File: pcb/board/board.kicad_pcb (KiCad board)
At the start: 2 copper layers, 6 parts, among them J1 Screw_Terminal_01x03, J2 Screw_Terminal_01x03, J3 Screw_Terminal_01x03, J5 Screw_Terminal_01x03

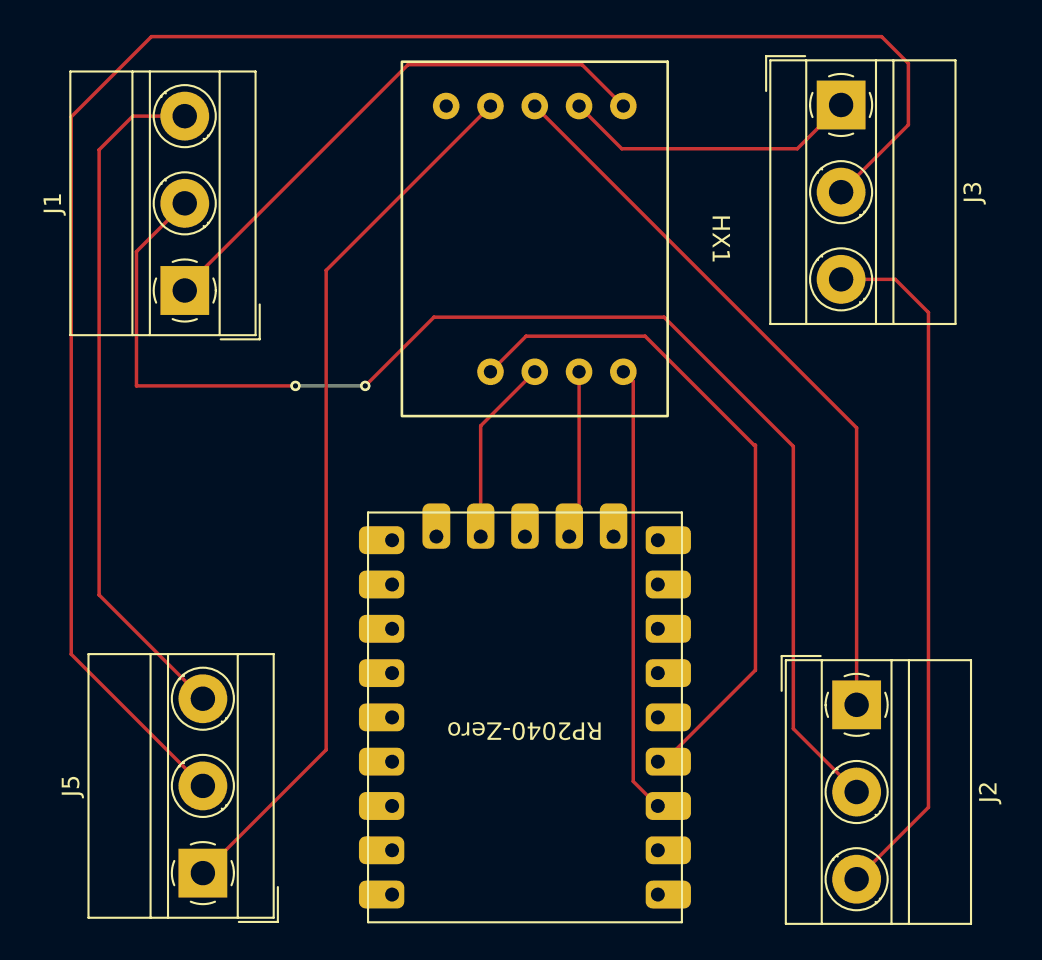
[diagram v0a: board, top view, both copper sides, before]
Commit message: wip work on the load cell part
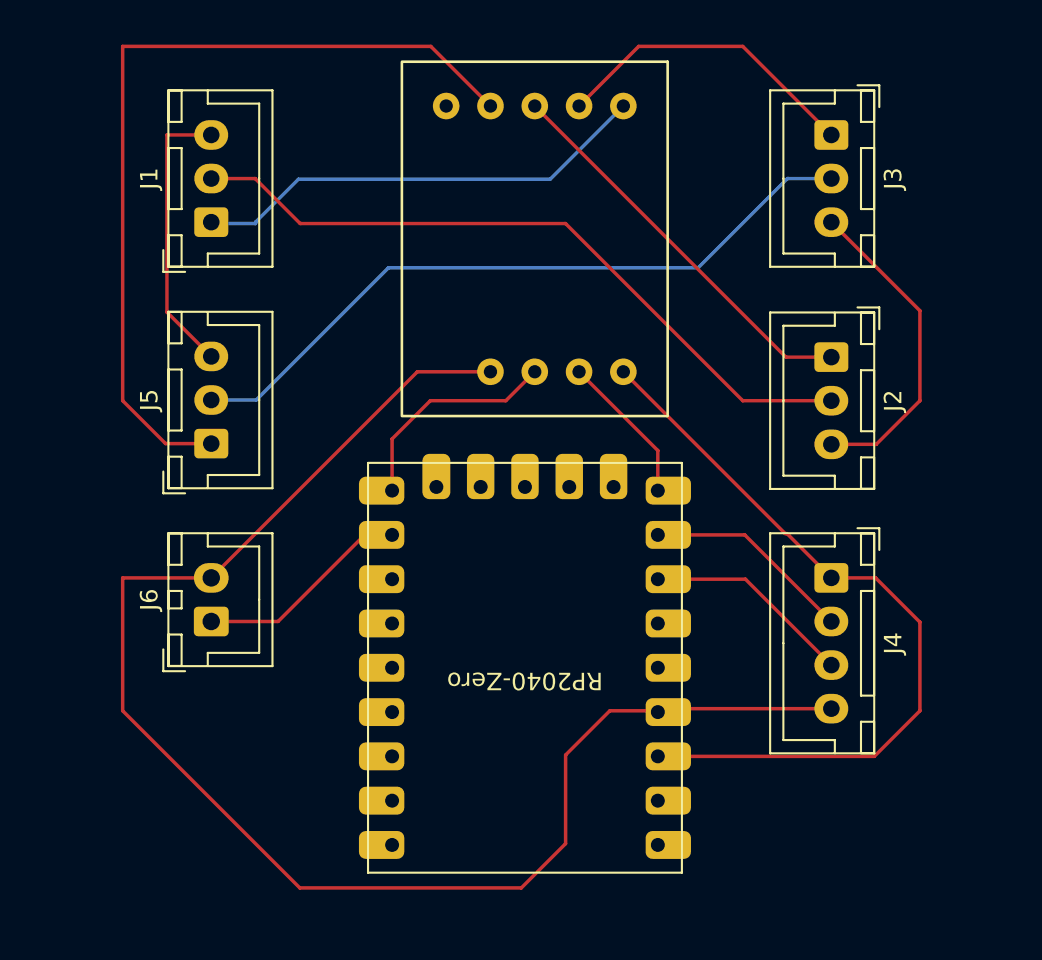
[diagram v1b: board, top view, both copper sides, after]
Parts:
- added J4: Screw_Terminal_01x04, Connector_JST:JST_XH_B4B-XH-A_1x04_P2.50mm_Vertical, F.Cu at (167.6, 66.0)
- added J6: Screw_Terminal_01x02, Connector_JST:JST_XH_B2B-XH-A_1x02_P2.50mm_Vertical, F.Cu at (132.1, 68.5)
- J1, J2, J3, J5: footprint TerminalBlock_MetzConnect:TerminalBlock_MetzConnect_Type011_RT05503HBWC_1x03_P5.00mm_Horizontal -> Connector_JST:JST_XH_B3B-XH-A_1x03_P2.50mm_Vertical
- moved J5 24.6 mm to (132.1, 58.3)
- moved J2 20.0 mm to (167.6, 53.4)
- moved J1 4.20 mm to (132.1, 45.6)
- moved RZ1 2.85 mm to (160.2, 58.5)
- moved J3 1.81 mm to (167.6, 40.6)
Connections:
- net Net-(HX1-2.7-5v) renamed 3V3
- net Net-(HX1-GND) renamed GND
- RZ1 pad 11: Net-(HX1-CLK) -> unconnected-(RZ1-GP10-Pad11)
- RZ1 pad 13: Net-(HX1-DAT) -> unconnected-(RZ1-GP12-Pad13)
- RZ1 pad 15: unconnected-(RZ1-GP14-Pad15) -> Net-(HX1-DAT)
- RZ1 pad 16: unconnected-(RZ1-GP15-Pad16) -> Net-(J4-Pin_2)
- RZ1 pad 17: unconnected-(RZ1-GP26-Pad17) -> Net-(J4-Pin_3)
- RZ1 pad 8: unconnected-(RZ1-GP7-Pad8) -> Net-(J6-Pin_1)
- RZ1 pad 9: unconnected-(RZ1-GP8-Pad9) -> Net-(HX1-CLK)
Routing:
- net Net-(J3-Pin_2): track 101.0 -> 40.8 mm
- net GND: track 39.3 -> 85.8 mm
- net Net-(J1-Pin_2): track 75.4 -> 40.8 mm, vias 2 -> 0
- net Net-(J1-Pin_3): track 39.7 -> 16.3 mm
- net Net-(J2-Pin_3): track 40.0 -> 18.5 mm
- net Net-(HX1-WHT/A-): track 42.0 -> 23.0 mm
- net 3V3: track 25.7 -> 44.1 mm
- net Net-(J6-Pin_1): track 0.00 -> 12.4 mm
- net Net-(J4-Pin_2): track 0.00 -> 12.0 mm
- net Net-(J4-Pin_3): track 0.00 -> 12.0 mm
- net Net-(HX1-RED/E+): track 31.4 -> 26.5 mm
- net Net-(HX1-CLK): track 10.7 -> 12.7 mm
- net Net-(HX1-GRN/A+): track 50.8 -> 48.9 mm
- net Net-(HX1-DAT): track 9.68 -> 8.69 mm
- net Net-(HX1-BLK/E-): track 17.1 -> 18.0 mm
